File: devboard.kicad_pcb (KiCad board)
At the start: 4 copper layers, 132.1 x 62.2 mm, 91 parts, among them J1 Conn_01x04, J2 Conn_02x05_Odd_Even, J3 USB_B_Micro, J4 Conn_01x04, J5 Conn_02x10_Counter_Clockwise, J6 Conn_02x04_Counter_Clockwise, Q1 Q_NPN_BEC, Q2 Q_NPN_BEC, SW1 SW_SPST, U1 ATmega128L-8AU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

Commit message: Labeling correction
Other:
- board text added: "DaVinci Payload Two Devboard"
- board text removed: "DaVinci Payload Two"

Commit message: Fix pullup connections and minor silk alterations
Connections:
- R10 pad 1: Net-(R10-Pad1) -> Net-(C10-Pad1)
- R8 pad 1: Net-(R8-Pad1) -> Net-(C10-Pad1)
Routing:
- net Net-(C10-Pad1): track 137.4 -> 160.4 mm
- net /~WE: track 198.5 -> 199.0 mm

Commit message: Add power indicator and improve silk
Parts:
- added D11: PWRLED, LED_SMD:LED_0603_1608Metric_Castellated, F.Cu at (197.5, 79.4)
- added R13: 1k, Resistor_SMD:R_0603_1608Metric_Pad0.98x0.95mm_HandSolder, F.Cu at (197.4, 81.2)
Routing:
- net Net-(D11-Pad2): track 0.00 -> 1.94 mm
- net GND: track 247.3 -> 249.0 mm, vias 63 -> 64
- net VCC: track 79.8 -> 81.5 mm, vias 10 -> 11
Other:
- board text added: "+5V"
- board text added: "BANK 1"
- board text added: "BANK 2"
- board text added: "BANK1_EN"
- board text added: "BANK2_EN"
- board text added: "M1_CE2"
- board text added: "M2_CE2"
- board text added: "M3_CE2"
- board text added: "M4_CE2"
- board text added: "M5_CE2"
- board text added: "M6_CE2"
- board text added: "PWR"
- board text added: "RX|TX"
- board text added: "WDI"
- board text added: "~RST"

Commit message: Net cleanup
Ran the KiCAD net cleanup tool with all options enabled. This created
a lot of commit noise, but none of this functionally changes the circit.
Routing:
- net /A1: track 265.3 -> 251.7 mm, vias 5 -> 4
- net /A0: track 272.7 -> 259.1 mm, vias 5 -> 4
- net GND: track 249.0 -> 246.1 mm
- net Net-(R27-Pad2): track 44.3 -> 43.6 mm
- net /~RST: track 88.2 -> 87.7 mm

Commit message: SPI programming and silk improvements
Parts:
- added J7: Conn_02x03_Counter_Clockwise, Connector_PinHeader_1.27mm:PinHeader_2x03_P1.27mm_Vertical, F.Cu at (176.0, 69.7)
- added TP12: TestPoint, Connector_PinHeader_2.54mm:PinHeader_1x01_P2.54mm_Vertical, F.Cu at (168.5, 73.7)
- moved U2 0.51 mm to (165.5, 91.3)
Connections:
- U1 pad 1: Net-(U1-Pad1) -> /~PEN
- U1 pad 10: /A19 -> Net-(U1-Pad10)
- U1 pad 11: /A18 -> /SCK
- U1 pad 2: /~OE -> /MOSI
- U1 pad 3: /~WE -> /MISO
- U1 pad 4: Net-(U1-Pad4) -> /~OE
- U1 pad 5: Net-(U1-Pad5) -> /~WE
- U1 pad 7: Net-(U1-Pad7) -> /A19
- U1 pad 8: Net-(U1-Pad8) -> /A18
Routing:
- net /SCK: track 0.00 -> 29.1 mm, vias 0 -> 4
- net /MOSI: track 0.00 -> 25.8 mm, vias 0 -> 4
- net /MISO: track 0.00 -> 21.8 mm, vias 0 -> 4
- net /~PEN: track 0.00 -> 13.5 mm, vias 0 -> 3
- net /M3_CE2: track 69.2 -> 79.4 mm
- net /M1_CE2: track 152.7 -> 159.6 mm
- net /BANK2_EN: track 21.8 -> 27.4 mm
- net /~RST: track 87.7 -> 91.7 mm
- net /WDI: track 9.73 -> 12.9 mm, vias 0 -> 2
- net /A6: track 250.6 -> 253.4 mm
- net /A19: track 262.8 -> 264.4 mm
- net VCC: track 81.5 -> 82.9 mm, vias 11 -> 12
- net /~OE: track 202.2 -> 200.8 mm
- net /~WE: track 199.0 -> 200.2 mm
- net GND: track 246.1 -> 247.3 mm, vias 64 -> 65
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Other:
- board text added: "~PEN"

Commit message: Add crystal pads, MCU LED, fix serial routing
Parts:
- added D12: STATLED, LED_SMD:LED_0603_1608Metric_Castellated, F.Cu at (172.7, 70.3)
- added R14: 1k, Resistor_SMD:R_0603_1608Metric_Pad0.98x0.95mm_HandSolder, F.Cu at (171.2, 70.3)
- added TP13: TestPoint, TestPoint:TestPoint_Bridge_Pitch2.54mm_Drill0.7mm, F.Cu at (178.1, 106.3)
- added TP14: TestPoint, TestPoint:TestPoint_Bridge_Pitch2.54mm_Drill0.7mm, F.Cu at (175.5, 106.3)
- moved TP7 5.21 mm to (168.5, 70.0)
- moved C4 3.71 mm to (173.4, 106.0), turned to 270 degrees
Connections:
- J1 pad 2: /UART_TX -> /UART_RX
- J1 pad 3: /UART_RX -> /UART_TX
- U1 pad 27: /A3 -> /UART_RX
- U1 pad 29: /UART_RX -> /A3
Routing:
- net Net-(D12-Pad1): track 0.00 -> 15.6 mm
- net GND: track 247.3 -> 262.8 mm, vias 65 -> 66
- net /~RST: track 91.7 -> 102.0 mm
- net /SDA: track 36.1 -> 29.9 mm
- net /A8: track 245.4 -> 248.3 mm
- net /A15: track 261.1 -> 264.1 mm
- net Net-(D12-Pad2): track 0.00 -> 2.37 mm
- net /UART_RX: track 36.4 -> 38.2 mm, vias 1 -> 2
- net /M4_CE2: track 115.1 -> 116.4 mm
- net /A3: track 247.2 -> 246.0 mm, vias 4 -> 5
- net /M3_CE2: track 79.4 -> 80.6 mm
- net VCC: track 82.9 -> 84.0 mm, vias 12 -> 13
- net /SCL: track 49.1 -> 48.9 mm, vias 3 -> 1

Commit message: Add more testpoints
Just in case the Cypress chip operates differently than advertised.
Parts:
- added TP15: TestPoint, TestPoint:TestPoint_Pad_D1.5mm, F.Cu at (82.9, 73.5)
- added TP16: TestPoint, TestPoint:TestPoint_Pad_D1.5mm, F.Cu at (82.8, 102.0)
- added TP17: TestPoint, Connector_PinHeader_2.54mm:PinHeader_1x01_P2.54mm_Vertical, F.Cu at (148.8, 70.0)
- added TP18: TestPoint, Connector_PinHeader_2.54mm:PinHeader_1x01_P2.54mm_Vertical, F.Cu at (82.5, 116.2)
- added TP19: TestPoint, TestPoint:TestPoint_Pad_D1.5mm, F.Cu at (106.7, 73.9)
- added TP20: TestPoint, TestPoint:TestPoint_Pad_D1.5mm, F.Cu at (110.1, 107.6)
- added TP21: TestPoint, TestPoint:TestPoint_Pad_D1.5mm, F.Cu at (158.5, 74.9)
- added TP22: TestPoint, TestPoint:TestPoint_Pad_D1.5mm, F.Cu at (134.1, 101.9)
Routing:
- net Net-(R27-Pad2): track 43.6 -> 49.2 mm
- net Net-(R5-Pad2): track 3.06 -> 7.75 mm
- net Net-(R12-Pad2): track 3.06 -> 7.49 mm
- net Net-(R28-Pad2): track 5.80 -> 9.82 mm
- net Net-(R24-Pad2): track 5.51 -> 8.64 mm
- net /~WE: track 200.2 -> 203.1 mm
- net Net-(R23-Pad2): track 5.49 -> 8.35 mm
- net /~OE: track 200.8 -> 203.3 mm
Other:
- board text added: "~OE"
- board text added: "~WE"

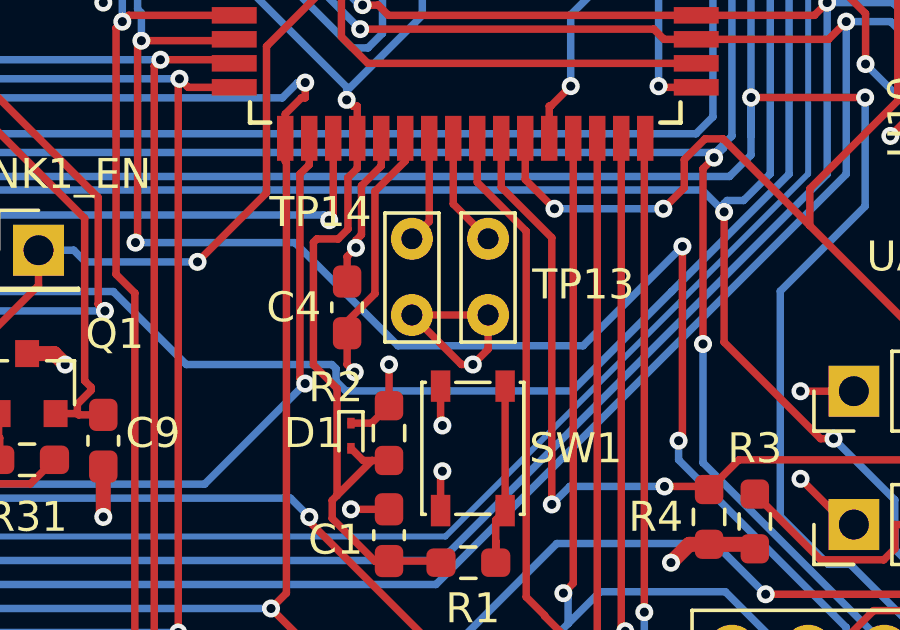
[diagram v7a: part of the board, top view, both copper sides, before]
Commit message: Small fixes to clock pads
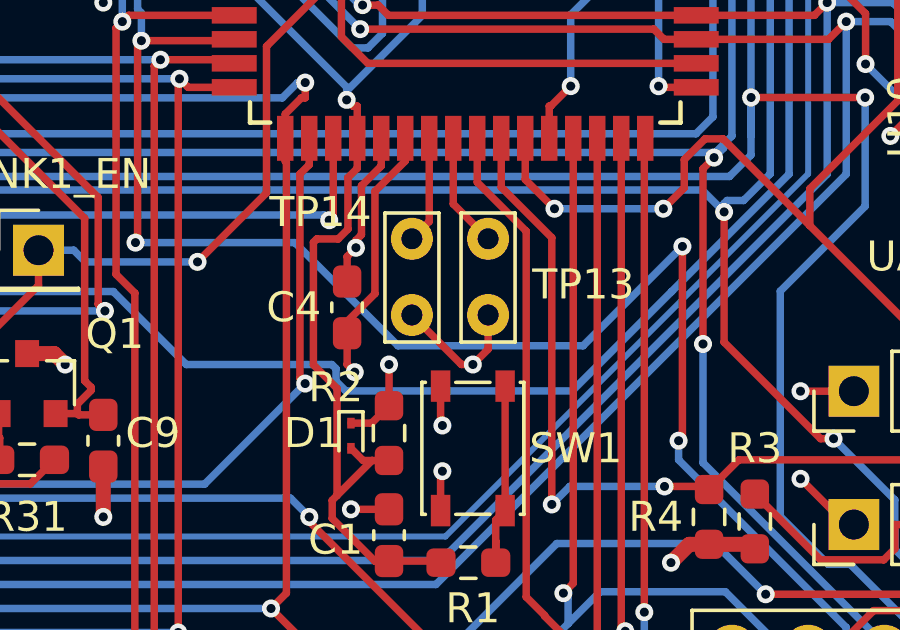
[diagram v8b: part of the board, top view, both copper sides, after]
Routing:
- net GND: track 262.8 -> 260.3 mm
